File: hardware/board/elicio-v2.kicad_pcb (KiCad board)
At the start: 4 copper layers, 17 x 33 mm, 67 parts, among them J1 TYPE-C-31-M-14, J2 SM02B-SRSS-TB, J3 HDR-3-RA, J4 TC2030-NL, P1 SIG1, P2 SIG2, P3 REF, Q1 AO3401A, Q2 2N7002, Q3 2N7002, Q4 2N7002, Q5 2N7002, SW1 4.5x4.5x1.6, U1 MDBT50Q-1MV2, U2 ADS1292IRSMT, U3 BQ25100YFPR, U4 TLV71330PDBVR, U5 USBLC6-2SC6

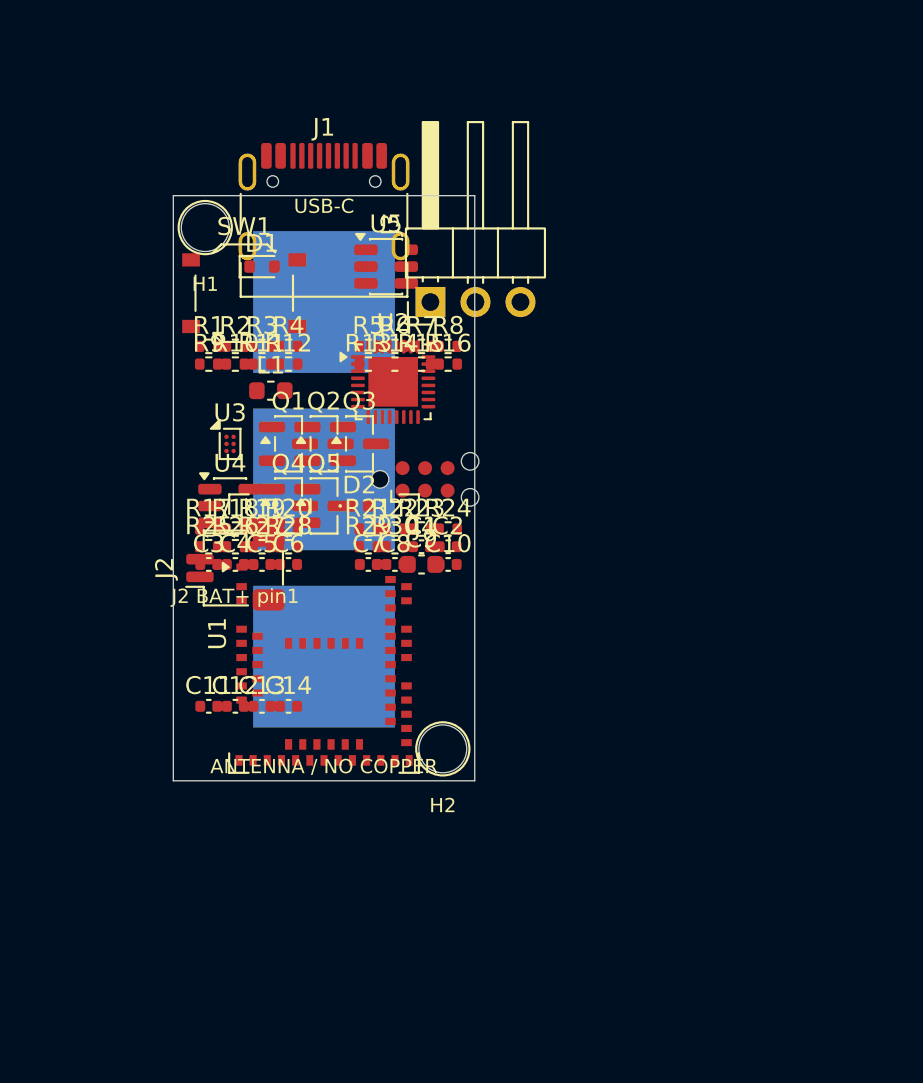
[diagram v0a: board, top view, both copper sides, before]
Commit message: board(v2): flex layout for interface II from WP11 winner
WP11 closed interface I at 0 runs, so the board is the 2-layer flex with ring-pad tabs on A_501015_series_w20.

Co-authored-by: Cursor <cursoragent@cursor.com>
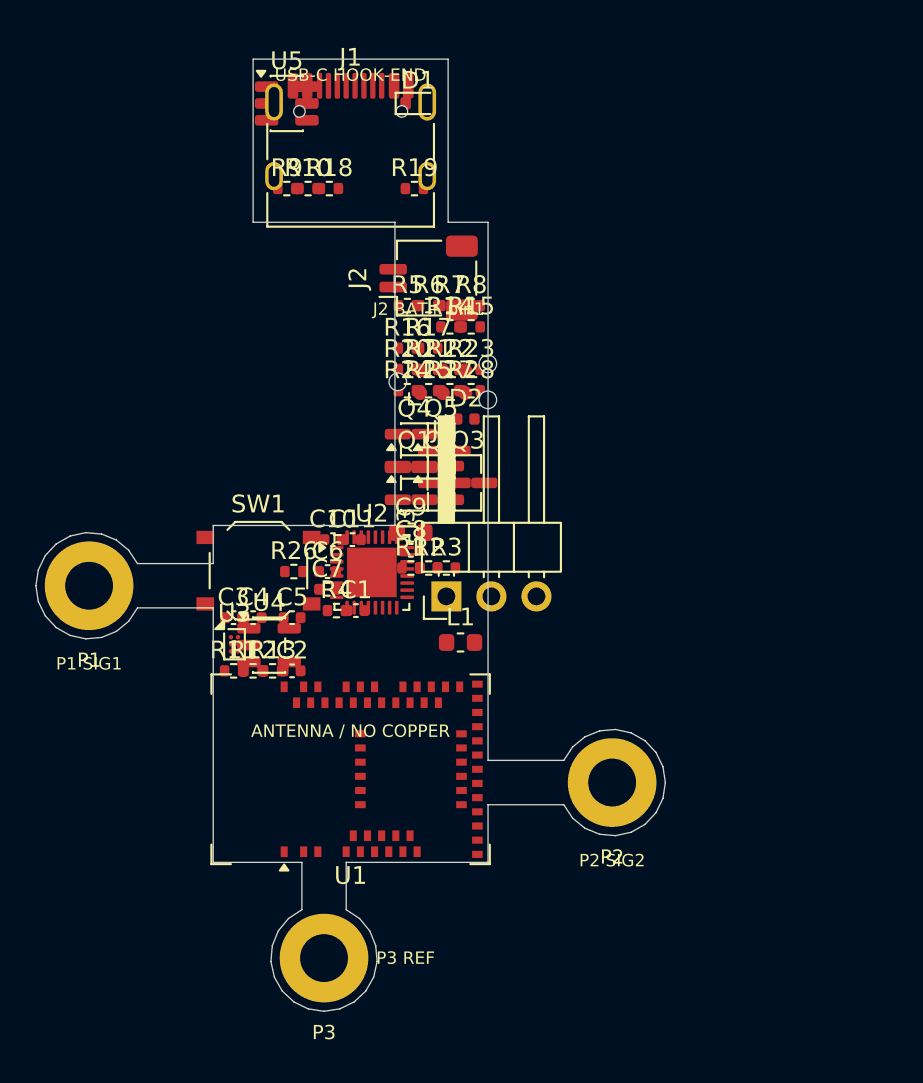
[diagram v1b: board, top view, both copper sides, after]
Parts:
- removed C12: 100nF, C_0402_1005Metric
- removed C13: 1uF, C_0402_1005Metric
- removed C14: 4.7uF, C_0402_1005Metric
- removed H1, H2: M2.5, MountingHole_M2.5
- removed R29, R30: 10M, R_0402_1005Metric
- P1, P2, P3: footprint PAD_8x8_ENIG -> RING_PAD_D5_H2.7; moved to F.Cu
- moved P2 23.6 mm to (24.8, 33.1)
- moved R19 21.0 mm to (13.6, -0.40)
- moved P1 20.8 mm to (-4.75, 22.0)
- moved R18 19.9 mm to (8.80, -0.40)
- moved J2 19.7 mm to (14.4, 4.65)
- moved R13 18.1 mm to (5.60, 26.8)
- moved L1 17.8 mm to (16.2, 25.2)
- moved R12 17.4 mm to (4.50, 26.8)
- moved R11 17.4 mm to (3.40, 26.8)
- moved P3 17.0 mm to (8.50, 43.0)
- moved R1 16.9 mm to (13.4, 21.0)
- moved J3 16.6 mm to (15.4, 22.6)
- moved R2 16.6 mm to (14.4, 21.0)
- moved R3 16.3 mm to (15.4, 21.0)
- moved R17 16.1 mm to (14.4, 8.60)
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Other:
- board size 17 x 33 mm -> 35.5 x 53.7 mm
- copper layers 4 -> 2
- rule pad_to_mask_clearance: 0 -> 0.1
- board text added: "BEND R>=1.5 NO VIA/PART/STIFFENER"
- board text added: "Eco1 FR4 0.3 parts (WP11)"
- board text added: "Eco2 FR4 0.2 tab"
- board text added: "II FLEX A_501015_series_w20"
- board text added: "NECK BEND"
- board text added: "USB-C HOOK-END"
- board text removed: "PROVISIONAL 17x33"
- board text removed: "USB-C"

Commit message: review(WP12): ISET, LED, divider, ERC 0/0, RF keep-out, routed flag, record
- ISET: R25 + R28 (20 k to GND) sat in parallel with RISET 6.80 k, so
  IOUT was about 26.6 mA, not 19.85. R28 now pulls LED_EN down; R25 alone
  feeds the high-impedance AIN7.
- LED: Q4's gate moves from ISET (about 1 V) to LED_EN (P0.04, pin 20);
  anode from VBUS, not VBAT, so it no longer loads the charger output.
- Battery divider: R21 to GND, Q5 DNP. The low-side switch left P0.02 at
  VBAT through 1 MΩ when off, above VDD + 0.3.
- ERC 0 errors, 0 warnings: mismatched symbols moved into lib/elicio as
  their embedded copies (netlist unchanged); J3 footprint library name.
- PCB: removed the length-along-s RF rule area that covered 15 module
  pads; the u-end area stays. Q5 DNP. Stiffener note 0.4.
- LCSC: C25803, C25765 and C1525 were each on two values (R1-R3 220 k
  among them); those 18 lines are blank, UNVERIFIED, for G3.
- release.py: summary has routed, tracks, nets and pads without a net;
  --routed fails closed on DRC errors, unconnected items, netless pads or
  no tracks. STEP with models. Tests cover both.
- board-v2.md: G2 default-state sentence, ESD actually used, REGOUT0 and
  the probe at a 1.8/3.0 V target, standoff stack 4.81 (no nut), foam 0.5,
  I = 0/720, decoupling deviates, DRC truth (PCB not synced, not placed).

Co-Authored-By: Claude Opus 5 <noreply@anthropic.com>
Claude-Session: https://claude.ai/code/session_014BkJUsEH26eSo9ULozTgDM
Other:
- board text added: "Eco1 FR4 0.4 parts (review r5)"
- board text removed: "Eco1 FR4 0.3 parts (WP11)"
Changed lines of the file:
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@@
 			)
 		)
-		(attr smd)
+		(attr smd dnp)
 		(duplicate_pad_numbers_are_jumpers no)
 		(fp_line
@@
 	)
 	(gr_text "ANTENNA / NO COPPER"
-		(at 10 30.2 0)
+		(at 4.1 32.35 90)
 		(layer "F.SilkS")
 		(effects
@@
 		)
 	)
-	(gr_text "Eco1 FR4 0.3 parts (WP11)"
+	(gr_text "Eco1 FR4 0.4 parts (review r5)"
 		(at 10 36.4 0)
 		(layer "Eco1.User")
@@
 			)
 		)
-	)
-	(zone
-		(layers "F.Cu" "B.Cu")
-		(name "RF_NO_COPPER")
-		(hatch edge 0.5)
-		(connect_pads
-			(clearance 0)
-		)
-		(min_thickness 0.25)
-		(keepout
-			(tracks not_allowed)
-			(vias not_allowed)
-			(pads not_allowed)
-			(copperpour not_allowed)
-			(footprints allowed)
-		)
-		(placement
-			(enabled no)
-			(sheetname "")
-		)
-		(fill
-			(thermal_gap 0.5)
-			(thermal_bridge_width 0.5)
-			(island_removal_mode 0)
-		)
-		(polygon
-			(pts
-				(xy 3.8 33.8) (xy 16.2 33.8) (xy 16.2 37.6) (xy 3.8 37.6)
-			)
-		)

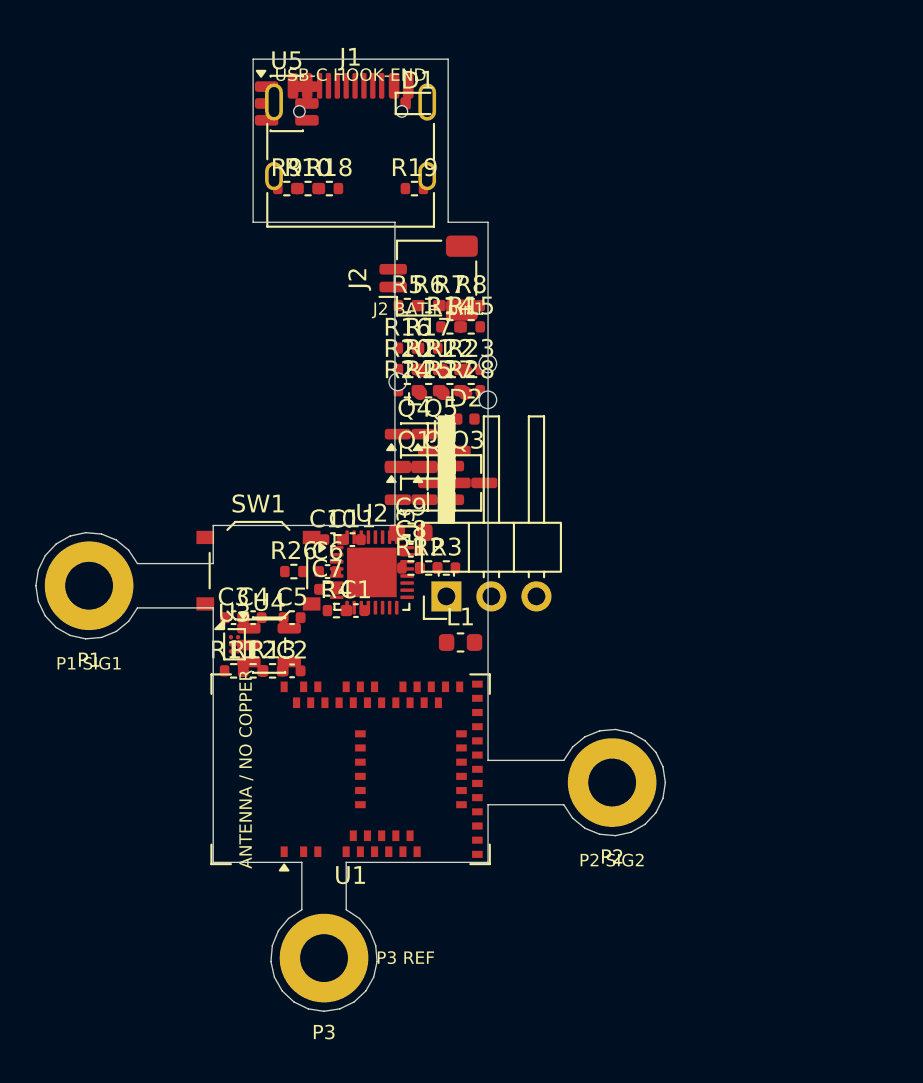
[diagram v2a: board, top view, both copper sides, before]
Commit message: board(v2b): placed from the packing, routed, released
Co-authored-by: Cursor <cursoragent@cursor.com>
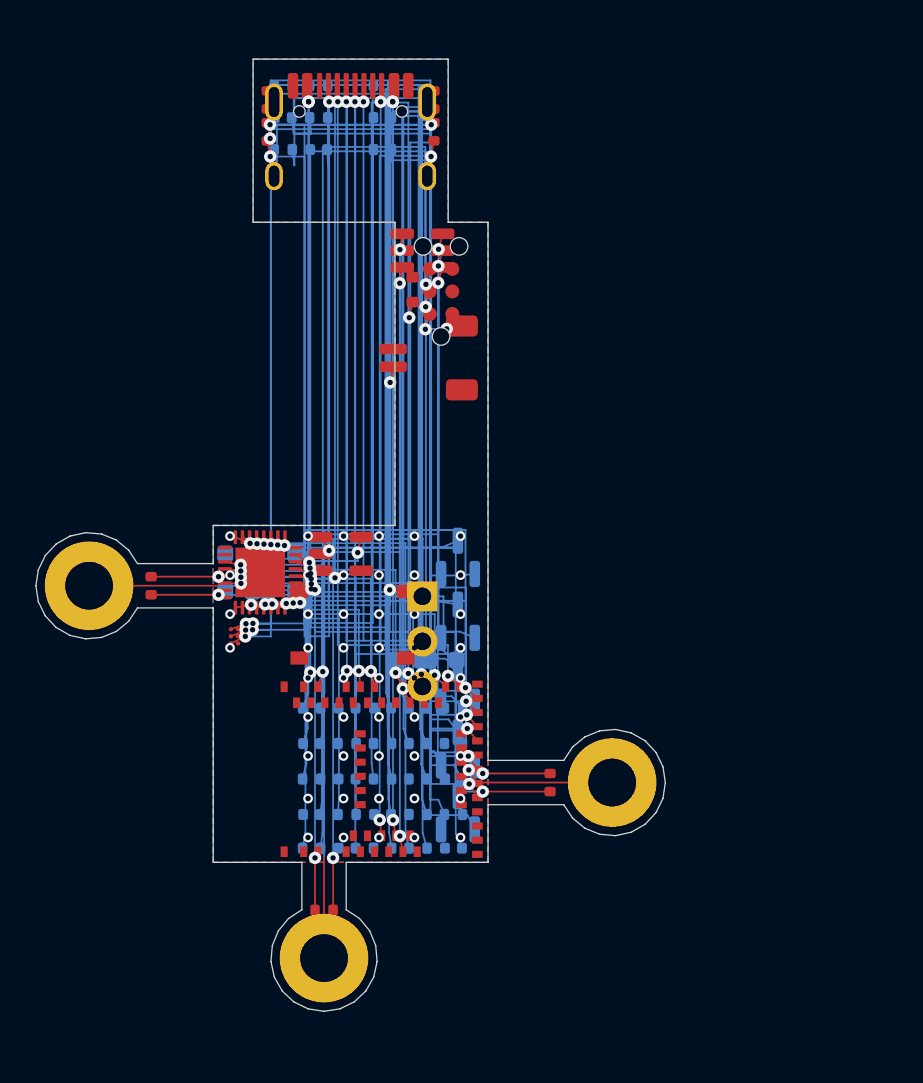
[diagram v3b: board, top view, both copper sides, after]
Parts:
- added C12: 100nF, C_0402_1005Metric, B.Cu at (11.8, 28.9)
- added C13: 1uF, C_0402_1005Metric, B.Cu at (11.8, 34.9)
- added C14: 4.7uF, C_0402_1005Metric, B.Cu at (9.80, 36.8)
- added C15: 100nF, C_0603_1608Metric, B.Cu at (6.10, 22.3)
- added R29: 10M, R_0402_1005Metric, B.Cu at (11.8, -4.40)
- added R30: 10M, R_0402_1005Metric, B.Cu at (11.8, -2.60)
- C1, C10, C11, C2, C3, C4, C5, C9, D2, L1, Q1, Q2, Q3, Q4, Q5, R11, R12, R13, R14, R15, R16, R17, R20, R21, R22, R23, R24, R25, R26, R27, R28, R4, R5, R6, R7, R8: moved to B.Cu
- C6: value 1uF -> 10uF; footprint C_0402_1005Metric -> C_0603_1608Metric; moved to B.Cu
- C7: footprint C_0402_1005Metric -> C_0603_1608Metric; moved to B.Cu
- C8: value 100nF -> 10uF; footprint C_0402_1005Metric -> C_0603_1608Metric; moved to B.Cu
- moved R6 29.1 mm to (9.80, 34.9), turned to 180 degrees
- moved C5 28.2 mm to (6.20, -4.40), turned to 180 degrees
- moved R8 27.2 mm to (11.8, 32.9), turned to 180 degrees
- moved R27 27.0 mm to (7.80, 36.8), turned to 180 degrees
- moved C4 26.7 mm to (8.20, -2.60), turned to 180 degrees
- moved R28 26.3 mm to (11.8, 36.8), turned to 180 degrees
- moved R21 25.1 mm to (13.8, 34.9), turned to 180 degrees
- moved R15 23.7 mm to (13.8, 30.9), turned to 180 degrees
- moved R25 22.9 mm to (7.80, 32.9), turned to 180 degrees
- moved R7 22.7 mm to (15.8, 28.9), turned to 180 degrees
- moved R22 20.6 mm to (7.80, 28.9), turned to 180 degrees
- moved R3 20.5 mm to (8.50, 40.3)
- moved Q5 20.4 mm to (16.1, 34.8), turned to 90 degrees
- moved D2 20.3 mm to (15.8, 32.9), turned to 180 degrees
- moved R24 20.2 mm to (9.80, 30.9), turned to 180 degrees
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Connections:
- C1 pad 1: (no net) -> RLD_FB
- C1 pad 2: (no net) -> RLDINV
- C10 pad 1: (no net) -> VCAP1
- C10 pad 2: (no net) -> GND
- C11 pad 1: (no net) -> VCAP2
- C11 pad 2: (no net) -> GND
- C2 pad 1: (no net) -> ISET
- C2 pad 2: (no net) -> GND
- C3 pad 1: (no net) -> VBUS
- C3 pad 2: (no net) -> GND
- C4 pad 1: (no net) -> VBAT
- C4 pad 2: (no net) -> GND
- C5 pad 1: (no net) -> AFE_VIN
- C5 pad 2: (no net) -> GND
- C6 pad 1: (no net) -> +3V0
- C6 pad 2: (no net) -> GND
- C7 pad 1: (no net) -> +3V0
- C7 pad 2: (no net) -> GND
- C8 pad 1: (no net) -> +3V0
- C8 pad 2: (no net) -> GND
- C9 pad 1: (no net) -> VREFP
- C9 pad 2: (no net) -> GND
- D1 pad 1: (no net) -> VBUS
- D1 pad 2: (no net) -> GND
- D2 pad 1: (no net) -> CHG_LED_K
- D2 pad 2: (no net) -> D2_A
- J1 pad : (no net) -> NC-J1-
- J1 pad A1: (no net) -> GND
- J1 pad A12: (no net) -> GND
- J1 pad A4: (no net) -> VBUS
- J1 pad A5: (no net) -> CC1
- J1 pad A6: (no net) -> USB_DP
- J1 pad A7: (no net) -> USB_DN
- J1 pad A8: (no net) -> unconnected-(J1-SBU1-PadA8)
- J1 pad A9: (no net) -> VBUS
- J1 pad B1: (no net) -> GND
- J1 pad B12: (no net) -> GND
- J1 pad B4: (no net) -> VBUS
- J1 pad B5: (no net) -> CC2
- J1 pad B6: (no net) -> USB_DP
- J1 pad B7: (no net) -> USB_DN
- J1 pad B8: (no net) -> unconnected-(J1-SBU2-PadB8)
- J1 pad B9: (no net) -> VBUS
- J1 pad SH: (no net) -> GND
- J2 pad 1: (no net) -> VBAT
- J2 pad 2: (no net) -> GND
- J2 pad MP: (no net) -> GND
- J3 pad 1: (no net) -> SIG1
- J3 pad 2: (no net) -> SIG2
- J3 pad 3: (no net) -> REF
- J4 pad : (no net) -> NC-J4-
- J4 pad 1: (no net) -> +VDD
- J4 pad 2: (no net) -> SWDIO
- J4 pad 3: (no net) -> GND
- J4 pad 4: (no net) -> SWDCLK
- J4 pad 5: (no net) -> GND
- J4 pad 6: (no net) -> nRESET
- L1 pad 1: (no net) -> DCCH
- L1 pad 2: (no net) -> +VDD
- Q1 pad 1: (no net) -> AFE_GATE
- Q1 pad 2: (no net) -> VBAT
- Q1 pad 3: (no net) -> AFE_VIN
- Q2 pad 1: (no net) -> Q2_G
- Q2 pad 2: (no net) -> GND
- Q2 pad 3: (no net) -> AFE_EN_HW
- Q3 pad 1: (no net) -> AFE_EN_HW
- Q3 pad 2: (no net) -> GND
- Q3 pad 3: (no net) -> AFE_GATE
- Q4 pad 1: (no net) -> LED_EN
- Q4 pad 2: (no net) -> GND
- Q4 pad 3: (no net) -> CHG_LED_K
- Q5 pad 1: (no net) -> BAT_MEAS_EN
- Q5 pad 2: (no net) -> GND
- Q5 pad 3: (no net) -> GND
- R1 pad 1: (no net) -> SIG1
- R1 pad 2: (no net) -> AFE_IN1P
- R10 pad 1: (no net) -> CC2
- R10 pad 2: (no net) -> GND
- R11 pad 1: (no net) -> ISET
- R11 pad 2: (no net) -> GND
- R12 pad 1: (no net) -> PRETERM
- R12 pad 2: (no net) -> GND
- R13 pad 1: (no net) -> TS
- R13 pad 2: (no net) -> GND
- R14 pad 1: (no net) -> VBAT
- R14 pad 2: (no net) -> AFE_GATE
- R15 pad 1: (no net) -> VBAT
- R15 pad 2: (no net) -> AFE_EN_HW
- R16 pad 1: (no net) -> VBUS
- R16 pad 2: (no net) -> Q2_G
- R17 pad 1: (no net) -> Q2_G
- R17 pad 2: (no net) -> GND
- R18 pad 1: (no net) -> VBUS
- R18 pad 2: (no net) -> VBUS_DET
- R19 pad 1: (no net) -> VBUS_DET
- R19 pad 2: (no net) -> GND
- R2 pad 1: (no net) -> SIG2
- R2 pad 2: (no net) -> AFE_IN1N
- R20 pad 1: (no net) -> VBAT
- R20 pad 2: (no net) -> VBAT_SENSE
- R21 pad 1: (no net) -> VBAT_SENSE
- R21 pad 2: (no net) -> GND
- R22 pad 1: (no net) -> VBUS
- R22 pad 2: (no net) -> D2_A
- R23 pad 1: (no net) -> AFE_RESET
- R23 pad 2: (no net) -> GND
- R24 pad 1: (no net) -> AFE_START
- R24 pad 2: (no net) -> GND
- R25 pad 1: (no net) -> ISET
- R25 pad 2: (no net) -> CHG_MON
- R26 pad 1: (no net) -> nRESET
- R26 pad 2: (no net) -> +VDD
- R27 pad 1: (no net) -> AFE_DRDY_AFE
- R27 pad 2: (no net) -> AFE_DRDY
- R28 pad 1: (no net) -> LED_EN
- R28 pad 2: (no net) -> GND
- R3 pad 1: (no net) -> REF
- R3 pad 2: (no net) -> RLD_FB
- R4 pad 1: (no net) -> RLD_FB
- R4 pad 2: (no net) -> RLDINV
- R5 pad 1: (no net) -> AFE_SCLK
- R5 pad 2: (no net) -> AFE_SCLK_AFE
- R6 pad 1: (no net) -> AFE_MOSI
- R6 pad 2: (no net) -> AFE_MOSI_AFE
- R7 pad 1: (no net) -> AFE_CS
- R7 pad 2: (no net) -> AFE_CS_AFE
- R8 pad 1: (no net) -> AFE_MISO_AFE
- R8 pad 2: (no net) -> AFE_MISO
- R9 pad 1: (no net) -> CC1
- R9 pad 2: (no net) -> GND
- SW1 pad 1: (no net) -> nRESET
- SW1 pad 2: (no net) -> GND
- U1 pad 1: (no net) -> GND
- U1 pad 10: (no net) -> unconnected-(U1-P0.29-Pad10)
- U1 pad 11: (no net) -> VBAT_SENSE
- U1 pad 12: (no net) -> CHG_MON
- U1 pad 13: (no net) -> unconnected-(U1-P0.28-Pad13)
- U1 pad 14: (no net) -> unconnected-(U1-P0.30-Pad14)
- U1 pad 15: (no net) -> GND
- U1 pad 16: (no net) -> unconnected-(U1-P0.27-Pad16)
- U1 pad 17: (no net) -> unconnected-(U1-P0.00-Pad17)
- U1 pad 18: (no net) -> unconnected-(U1-P0.01-Pad18)
- U1 pad 19: (no net) -> unconnected-(U1-P0.26-Pad19)
- U1 pad 2: (no net) -> GND
- U1 pad 20: (no net) -> LED_EN
- U1 pad 21: (no net) -> unconnected-(U1-P0.05-Pad21)
- U1 pad 22: (no net) -> AFE_MOSI
- U1 pad 23: (no net) -> unconnected-(U1-P0.07-Pad23)
- U1 pad 24: (no net) -> AFE_SCLK
- U1 pad 25: (no net) -> unconnected-(U1-P1.08-Pad25)
- U1 pad 26: (no net) -> unconnected-(U1-P1.09-Pad26)
- U1 pad 27: (no net) -> unconnected-(U1-P0.11-Pad27)
- U1 pad 28: (no net) -> +VDD
- U1 pad 29: (no net) -> unconnected-(U1-P0.12-Pad29)
- U1 pad 3: (no net) -> unconnected-(U1-P1.10-Pad3)
- U1 pad 30: (no net) -> VBAT
- U1 pad 31: (no net) -> DCCH
- U1 pad 32: (no net) -> VBUS
- U1 pad 33: (no net) -> GND
- U1 pad 34: (no net) -> USB_DN
- U1 pad 35: (no net) -> USB_DP
- U1 pad 36: (no net) -> unconnected-(U1-P0.14-Pad36)
- U1 pad 37: (no net) -> AFE_CS
- U1 pad 38: (no net) -> unconnected-(U1-P0.16-Pad38)
- U1 pad 39: (no net) -> AFE_MISO
- U1 pad 4: (no net) -> unconnected-(U1-P1.11-Pad4)
- U1 pad 40: (no net) -> nRESET
- U1 pad 41: (no net) -> AFE_DRDY
- U1 pad 42: (no net) -> unconnected-(U1-P0.19-Pad42)
- U1 pad 43: (no net) -> unconnected-(U1-P0.21-Pad43)
- U1 pad 44: (no net) -> AFE_START
- U1 pad 45: (no net) -> unconnected-(U1-P0.23-Pad45)
- U1 pad 46: (no net) -> AFE_RESET
- U1 pad 47: (no net) -> unconnected-(U1-P1.00-Pad47)
- U1 pad 48: (no net) -> VBUS_DET
- U1 pad 49: (no net) -> unconnected-(U1-P0.25-Pad49)
- U1 pad 5: (no net) -> unconnected-(U1-P1.12-Pad5)
- U1 pad 50: (no net) -> unconnected-(U1-P1.02-Pad50)
- U1 pad 51: (no net) -> SWDIO
- U1 pad 52: (no net) -> unconnected-(U1-P0.09-Pad52)
- U1 pad 53: (no net) -> SWDCLK
- U1 pad 54: (no net) -> unconnected-(U1-P0.10-Pad54)
- U1 pad 55: (no net) -> GND
- U1 pad 56: (no net) -> unconnected-(U1-P1.04-Pad56)
- U1 pad 57: (no net) -> unconnected-(U1-P1.06-Pad57)
- U1 pad 58: (no net) -> unconnected-(U1-P1.07-Pad58)
- U1 pad 59: (no net) -> unconnected-(U1-P1.05-Pad59)
- U1 pad 6: (no net) -> unconnected-(U1-P1.13-Pad6)
- U1 pad 60: (no net) -> unconnected-(U1-P1.03-Pad60)
- U1 pad 61: (no net) -> unconnected-(U1-P1.01-Pad61)
- U1 pad 7: (no net) -> unconnected-(U1-P1.14-Pad7)
- U1 pad 8: (no net) -> unconnected-(U1-P1.15-Pad8)
- U1 pad 9: (no net) -> BAT_MEAS_EN
- U2 pad : (no net) -> NC-U2-
- U2 pad 1: (no net) -> unconnected-(U2-PGA1N-Pad1)
- U2 pad 10: (no net) -> GND
- U2 pad 11: (no net) -> VCAP1
- U2 pad 12: (no net) -> +3V0
- U2 pad 13: (no net) -> GND
- U2 pad 14: (no net) -> +3V0
- U2 pad 15: (no net) -> AFE_RESET
- U2 pad 16: (no net) -> AFE_START
- U2 pad 17: (no net) -> unconnected-(U2-CLK-Pad17)
- U2 pad 18: (no net) -> AFE_CS_AFE
- U2 pad 19: (no net) -> AFE_MOSI_AFE
- U2 pad 2: (no net) -> unconnected-(U2-PGA1P-Pad2)
- U2 pad 20: (no net) -> AFE_SCLK_AFE
- U2 pad 21: (no net) -> AFE_MISO_AFE
- U2 pad 22: (no net) -> AFE_DRDY_AFE
- U2 pad 23: (no net) -> +3V0
- U2 pad 24: (no net) -> GND
- U2 pad 25: (no net) -> unconnected-(U2-GPIO2-Pad25)
- U2 pad 26: (no net) -> unconnected-(U2-GPIO1-Pad26)
- U2 pad 27: (no net) -> VCAP2
- U2 pad 28: (no net) -> RLDINV
- U2 pad 29: (no net) -> RLD_FB
- U2 pad 3: (no net) -> AFE_IN1N
- U2 pad 30: (no net) -> RLD_FB
- U2 pad 31: (no net) -> +3V0
- U2 pad 32: (no net) -> +3V0
- U2 pad 33: (no net) -> GND
- U2 pad 4: (no net) -> AFE_IN1P
- U2 pad 5: (no net) -> +3V0
- U2 pad 6: (no net) -> +3V0
- U2 pad 7: (no net) -> unconnected-(U2-PGA2N-Pad7)
- U2 pad 8: (no net) -> unconnected-(U2-PGA2P-Pad8)
- U2 pad 9: (no net) -> VREFP
- U3 pad A1: (no net) -> VBAT
- U3 pad A2: (no net) -> VBUS
- U3 pad B1: (no net) -> TS
- U3 pad B2: (no net) -> ISET
- U3 pad C1: (no net) -> PRETERM
- U3 pad C2: (no net) -> GND
- U4 pad 1: (no net) -> AFE_VIN
- U4 pad 2: (no net) -> GND
- U4 pad 3: (no net) -> AFE_VIN
- U4 pad 4: (no net) -> unconnected-(U4-NC-Pad4)
- U4 pad 5: (no net) -> +3V0
- U5 pad 1: (no net) -> USB_DP
- U5 pad 2: (no net) -> GND
- U5 pad 3: (no net) -> USB_DN
- U5 pad 4: (no net) -> USB_DN
- U5 pad 5: (no net) -> VBUS
- U5 pad 6: (no net) -> USB_DP
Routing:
- net VBAT: track 0.00 -> 275.1 mm, vias 0 -> 3
- net VBUS: track 0.00 -> 265.9 mm, vias 0 -> 9
- net +VDD: track 0.00 -> 206.8 mm, vias 0 -> 2
- net LED_EN: track 0.00 -> 121.1 mm, vias 0 -> 1
- net VBAT_SENSE: track 0.00 -> 117.1 mm, vias 0 -> 1
- net USB_DP: track 0.00 -> 116.8 mm, vias 0 -> 5
- net USB_DN: track 0.00 -> 115.6 mm, vias 0 -> 5
- net RLD_FB: track 0.00 -> 112.8 mm, vias 0 -> 3
- net AFE_VIN: track 0.00 -> 104.6 mm, vias 0 -> 2
- net AFE_EN_HW: track 0.00 -> 94.4 mm
- net AFE_GATE: track 0.00 -> 84.2 mm
- net BAT_MEAS_EN: track 0.00 -> 81.4 mm, vias 0 -> 1
- net PRETERM: track 0.00 -> 76.2 mm, vias 0 -> 1
- net TS: track 0.00 -> 75.7 mm, vias 0 -> 1
- net AFE_MISO: track 0.00 -> 73.3 mm, vias 0 -> 1
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- added copper zone on B.Cu, net GND
- added copper zone on F.Cu, net GND
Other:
- rule pad_to_mask_clearance: 0.1 -> 0
- board text added: "Eco1 FR4 0.4 #1 parts island"
- board text added: "Eco1 FR4 0.4 #2 USB+pocket"
- board text added: "NO TAB FR4; STANDOFF CLAMP Q58"
- board text removed: "ANTENNA / NO COPPER"
- board text removed: "Eco1 FR4 0.4 parts (review r5)"
- board text removed: "Eco2 FR4 0.2 tab"
- board text removed: "II FLEX A_501015_series_w20"
- board text removed: "J2 BAT+ pin1"
- board text removed: "P1 SIG1"
- board text removed: "P2 SIG2"
- board text removed: "P3 REF"
- board text removed: "USB-C HOOK-END"

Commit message: board(v2c): drop the shorting bus fallback
Co-authored-by: Cursor <cursoragent@cursor.com>
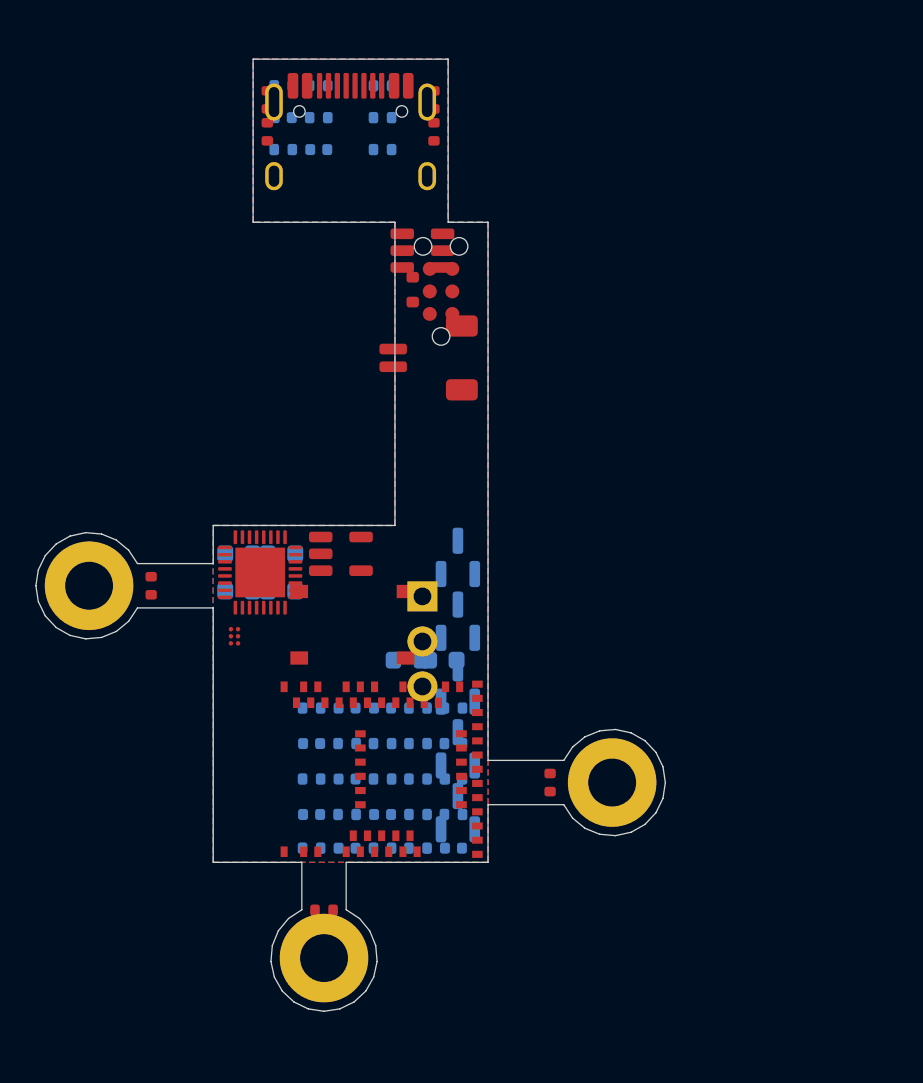
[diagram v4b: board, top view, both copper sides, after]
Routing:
- net VBAT: track 275.1 -> 0.00 mm, vias 3 -> 0
- net VBUS: track 265.9 -> 0.00 mm, vias 9 -> 0
- net +VDD: track 206.8 -> 0.00 mm, vias 2 -> 0
- net LED_EN: track 121.1 -> 0.00 mm, vias 1 -> 0
- net VBAT_SENSE: track 117.1 -> 0.00 mm, vias 1 -> 0
- net USB_DP: track 116.8 -> 0.00 mm, vias 5 -> 0
- net USB_DN: track 115.6 -> 0.00 mm, vias 5 -> 0
- net RLD_FB: track 112.8 -> 0.00 mm, vias 3 -> 0
- net AFE_VIN: track 104.6 -> 0.00 mm, vias 2 -> 0
- net AFE_EN_HW: track 94.4 -> 0.00 mm
- net AFE_GATE: track 84.2 -> 0.00 mm
- net BAT_MEAS_EN: track 81.4 -> 0.00 mm, vias 1 -> 0
- net PRETERM: track 76.2 -> 0.00 mm, vias 1 -> 0
- net TS: track 75.7 -> 0.00 mm, vias 1 -> 0
- net AFE_MISO: track 73.3 -> 0.00 mm, vias 1 -> 0
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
